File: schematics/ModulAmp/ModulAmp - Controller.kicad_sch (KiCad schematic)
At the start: 0 parts

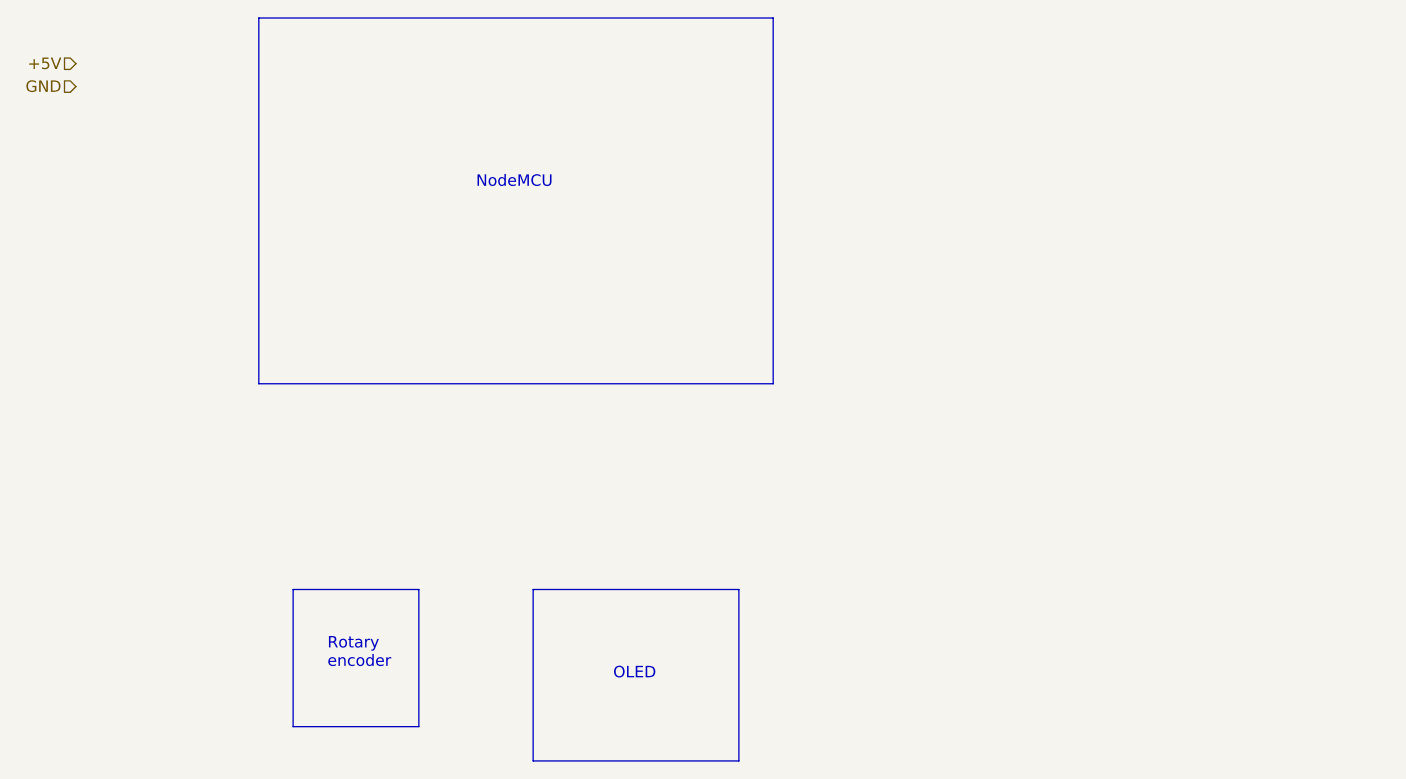
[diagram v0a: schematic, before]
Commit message: Refactored strings and added DHTxx full support
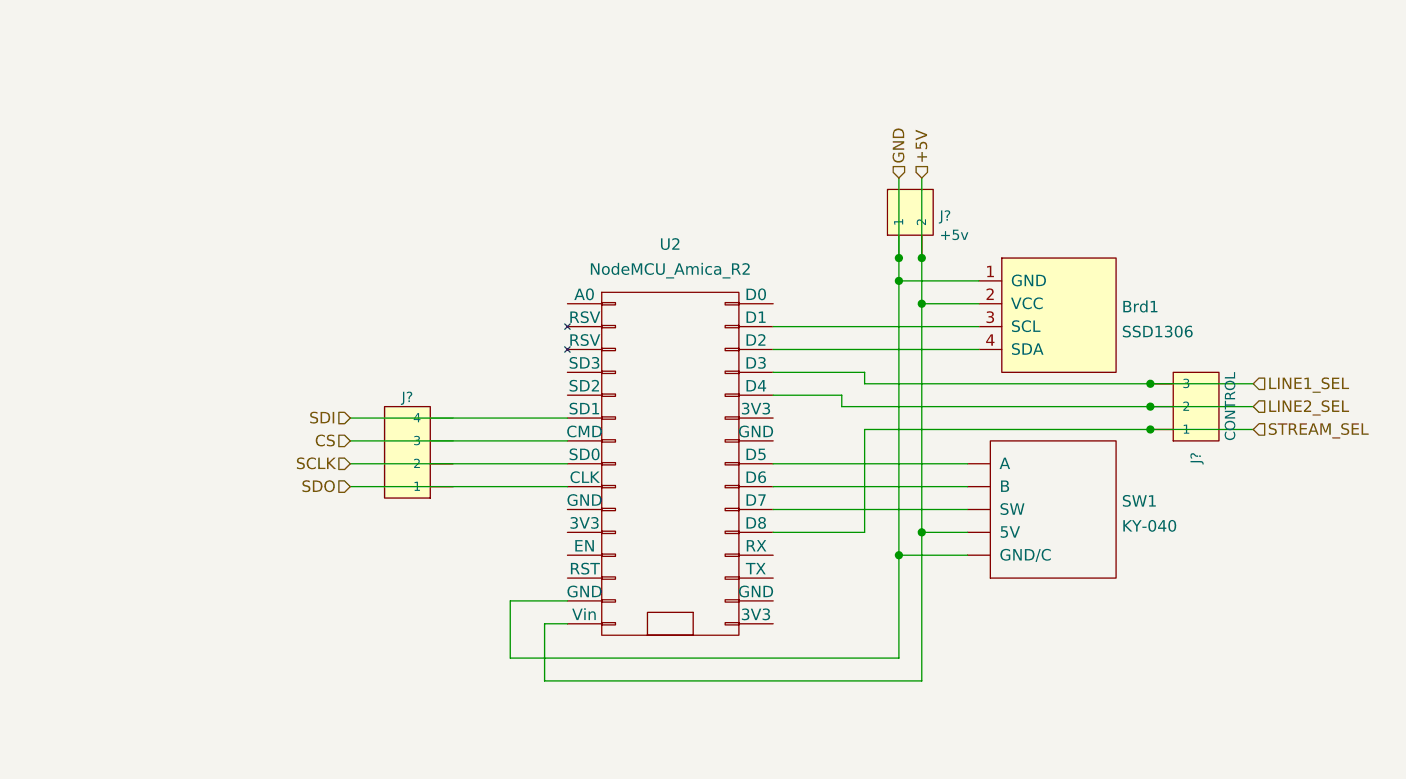
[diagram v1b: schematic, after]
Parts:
- added Brd1: SSD1306, symbol SSD1306-128x64_OLED:SSD1306
- added J?: CONN_04JST-PTH-VERT, JST-4-PTH-VERT, symbol SparkFun-Connectors:CONN_04JST-PTH-VERT
- added J?: +5v, JST-2-PTH, symbol SparkFun-Connectors:CONN_02JST-PTH-2
- added J?: CONTROL, JST-3-PTH-VERT, symbol SparkFun-Connectors:CONN_03JST-PTH-VERT
- added SW1: KY-040, symbol YEUTTERG_Generic:KY-040
- added U2: NodeMCU_Amica_R2, symbol nodemcu:NodeMCU_Amica_R2
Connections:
- net +5V: now also Brd1.2 (VCC), J?.2, SW1.~ (SW), U2.15 (Vin)
- net GND: now also Brd1.1 (GND), J?.1, SW1.~ (SW), U2.14 (GND)
- new net: SW1.~ (SW), U2.21 (D7)
- new net: SW1.~ (SW), U2.22 (D6)
- new net: SW1.~ (SW), U2.23 (D5)
- new net: Brd1.4 (SDA), U2.28 (D2)
- new net: Brd1.3 (SCL), U2.29 (D1)
- new net CS: U2.7 (CMD)
- new net LINE1_SEL: J?.3, U2.27 (D3)
- new net LINE2_SEL: J?.2, U2.26 (D4)
- new net SCLK: U2.8 (SD0)
- new net SDI: U2.6 (SD1)
- new net SDO: U2.9 (CLK)
- new net STREAM_SEL: J?.1, U2.20 (D8)
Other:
- note removed: "NodeMCU"
- note removed: "OLED"
- note removed: "Rotary encoder"
